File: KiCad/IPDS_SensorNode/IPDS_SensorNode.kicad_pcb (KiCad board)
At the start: 2 copper layers, 120 x 90 mm, 18 parts, among them J1 ESP32_Left, J2 ESP32_Right, J3 MPU6050, J4 DS3231_RTC, J5 NEO-6M_GPS, J6 USB_Micro_B

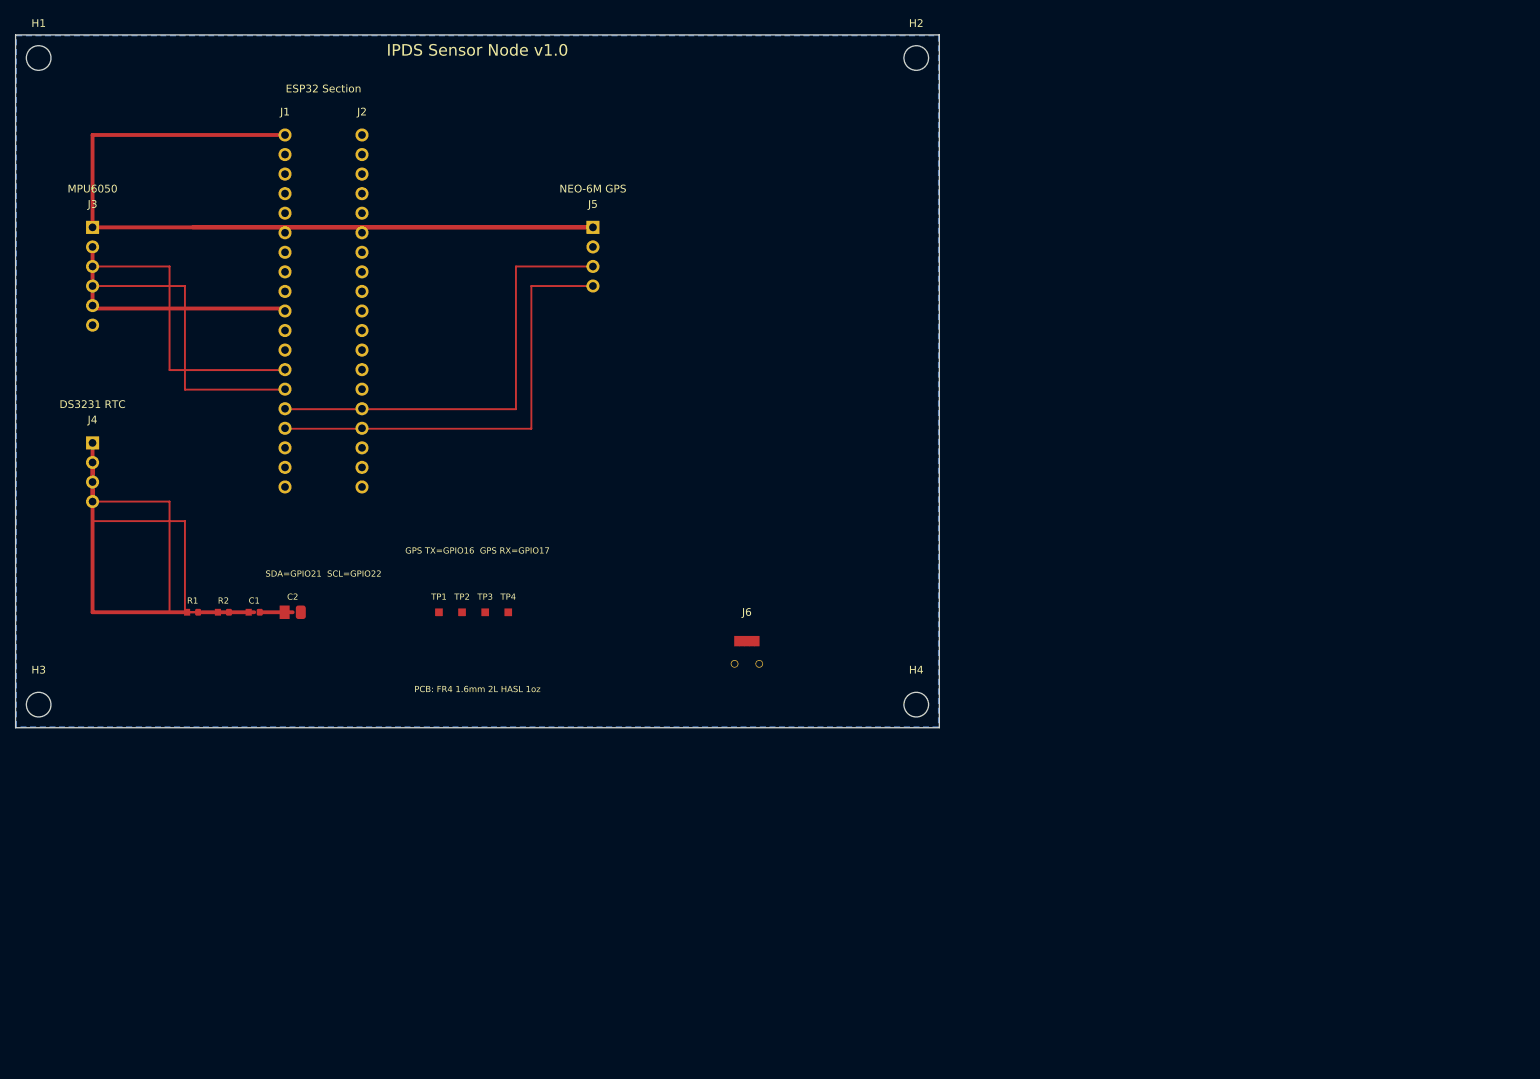
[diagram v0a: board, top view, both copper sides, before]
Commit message: Updated KiCad design - PCB and schematic improvements
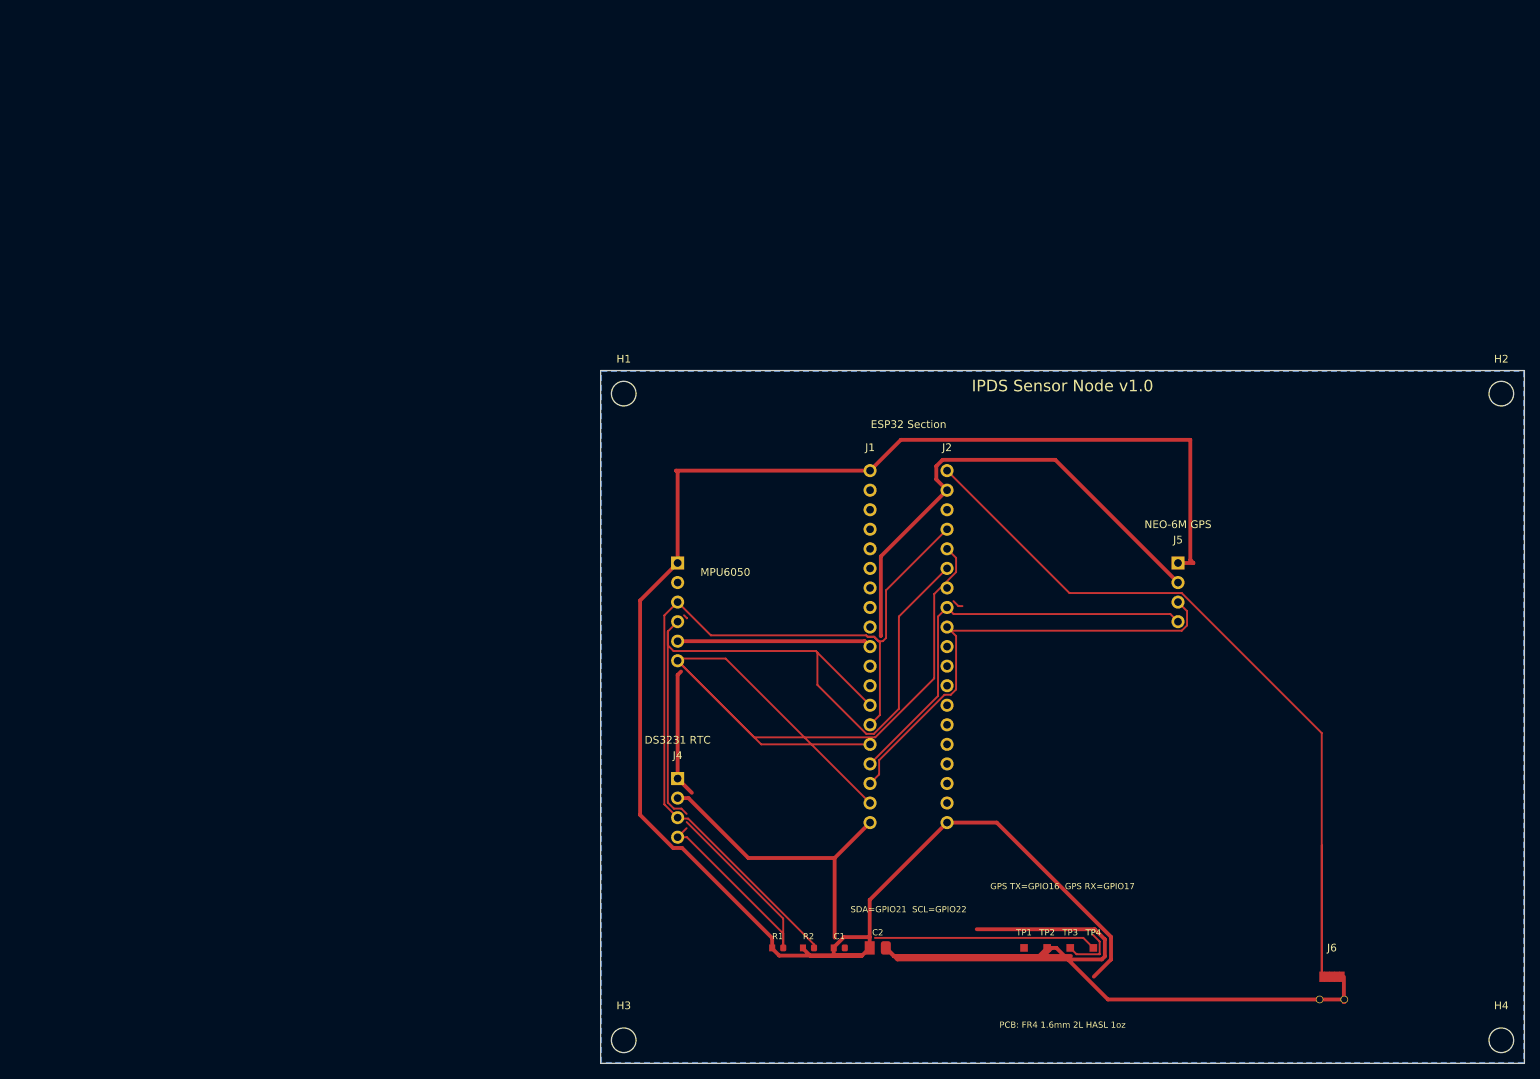
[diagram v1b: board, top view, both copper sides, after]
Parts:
- moved C1 87.6 mm to (112.0, 123.6)
- moved C2 87.6 mm to (117.0, 123.6)
- moved H1 87.6 mm to (84.0, 51.6)
- moved H2 87.6 mm to (198.0, 51.6)
- moved H3 87.6 mm to (84.0, 135.6)
- moved H4 87.6 mm to (198.0, 135.6)
- moved J1 87.6 mm to (116.0, 61.6)
- moved J2 87.6 mm to (126.0, 61.6)
- moved J3 87.6 mm to (91.0, 73.6)
- moved J4 87.6 mm to (91.0, 101.6)
- moved J5 87.6 mm to (156.0, 73.6)
- moved J6 87.6 mm to (176.0, 128.6)
- moved R1 87.6 mm to (104.0, 123.6)
- moved R2 87.6 mm to (108.0, 123.6)
- moved TP1 87.6 mm to (136.0, 123.6)
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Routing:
- net GND: track 48.5 -> 270.9 mm
- net (no net): track 0.00 -> 123.5 mm
- net VIN: track 0.00 -> 111.5 mm
- net SDA: track 66.6 -> 149.1 mm
- net SCL: track 68.0 -> 143.6 mm
- net +3V3: track 188.3 -> 260.8 mm
- net GPS_RX: track 58.5 -> 55.2 mm
- net GPS_TX: track 58.5 -> 61.1 mm
